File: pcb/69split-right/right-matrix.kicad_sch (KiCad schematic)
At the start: 80 parts, among them SW1 Y, SW10 I, SW11 K, SW12 <,,, SW13 Alt, SW14 (,9,,F9, SW15 O, SW16 L, SW17 >,., SW18 Fn, SW19 ),0,,F10, SW2 H, SW20 P, SW21 :,;, SW22 ?,/, SW23 Ctrl, SW24 _,-,,F11, SW25 {,[, SW26 ",', SW27 Shift, SW28 ←, SW29 +,=,,F12, SW3 N, SW30 },], SW31 Enter, SW32 ↑, SW33 ↓, SW34 Backspace, SW35 |,\, SW36 Home,PgUp, SW37 End,PgDn, SW38 →, SW39 Delete,Insert, SW4 Space, SW40 ~~,`, SW5 &,7,,F7, SW6 U, SW7 J, SW8 M, SW9 *,8,,F8

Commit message: Started layout?
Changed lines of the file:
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@@
 	)
 	(bus_entry
-		(at 196.85 134.62)
+		(at 199.39 134.62)
 		(size -2.54 2.54)
 		(stroke
@@
 	)
 	(bus_entry
-		(at 215.9 134.62)
+		(at 218.44 134.62)
 		(size -2.54 2.54)
 		(stroke
@@
 	)
 	(bus_entry
-		(at 156.21 134.62)
+		(at 158.75 134.62)
 		(size -2.54 2.54)
 		(stroke
@@
 	)
 	(bus_entry
-		(at 176.53 134.62)
+		(at 179.07 134.62)
 		(size -2.54 2.54)
 		(stroke
@@
 	)
 	(bus_entry
-		(at 137.16 134.62)
+		(at 139.7 134.62)
 		(size -2.54 2.54)
 		(stroke
@@
 	(bus
 		(pts
-			(xy 134.62 137.16) (xy 153.67 137.16)
-		)
-		(stroke
-			(width 0)
-			(type default)
-		)
-	)
-	(bus
-		(pts
-			(xy 173.99 137.16) (xy 194.31 137.16)
+			(xy 137.16 137.16) (xy 156.21 137.16)
+		)
+		(stroke
+			(width 0)
+			(type default)
+		)
+	)
+	(bus
+		(pts
+			(xy 176.53 137.16) (xy 196.85 137.16)
 		)
 		(stroke
@@
 	(bus
 		(pts
-			(xy 194.31 137.16) (xy 213.36 137.16)
+			(xy 196.85 137.16) (xy 215.9 137.16)
 		)
 		(stroke
@@
 	(bus
 		(pts
-			(xy 153.67 137.16) (xy 173.99 137.16)
+			(xy 156.21 137.16) (xy 176.53 137.16)
 		)
 		(stroke
@@
 	(bus
 		(pts
-			(xy 213.36 137.16) (xy 234.95 137.16)
+			(xy 215.9 137.16) (xy 234.95 137.16)
 		)
 		(stroke
@@
 	(bus
 		(pts
-			(xy 115.57 137.16) (xy 134.62 137.16)
-		)
-		(stroke
+			(xy 115.57 137.16) (xy 137.16 137.16)
+		)
+		(stroke

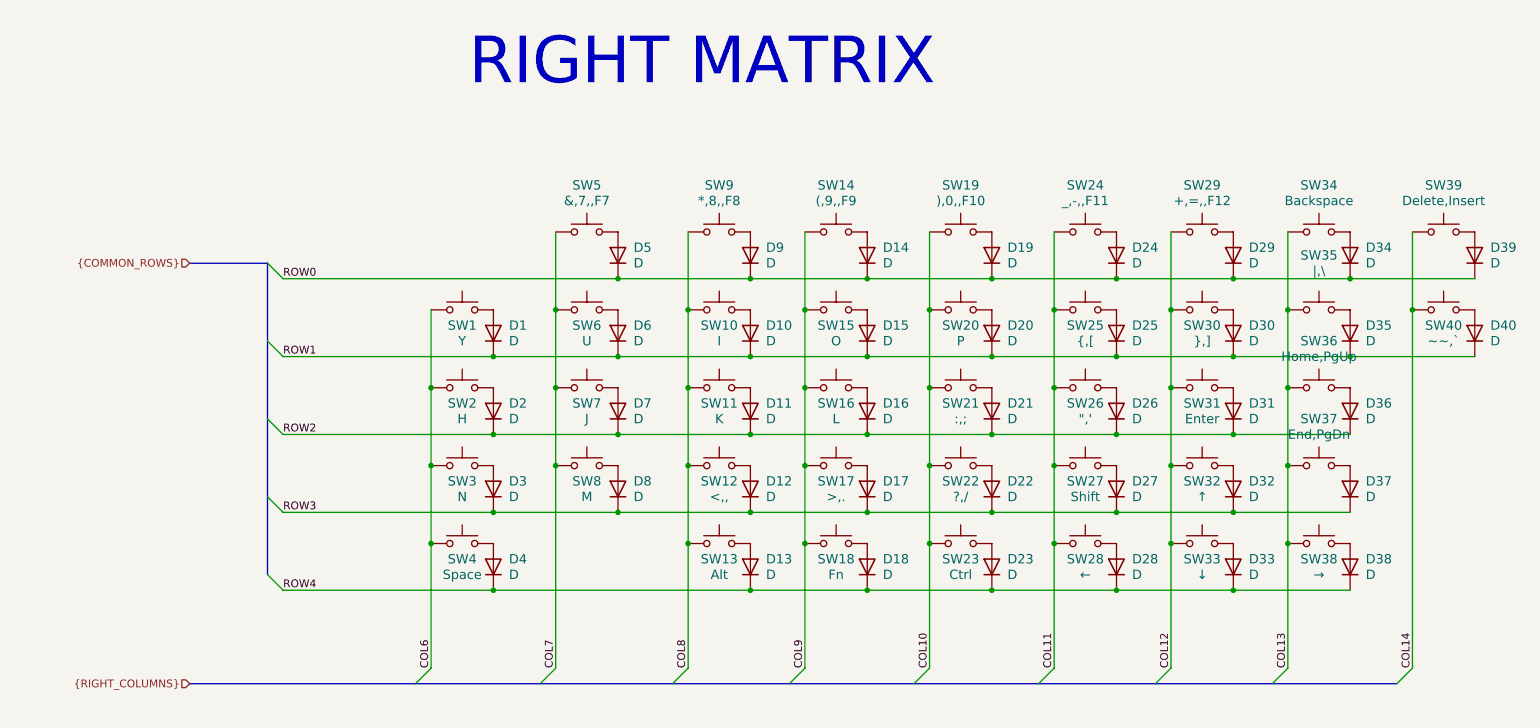
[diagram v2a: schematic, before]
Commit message: Started changing things gain to use an I/O expander with I2C.
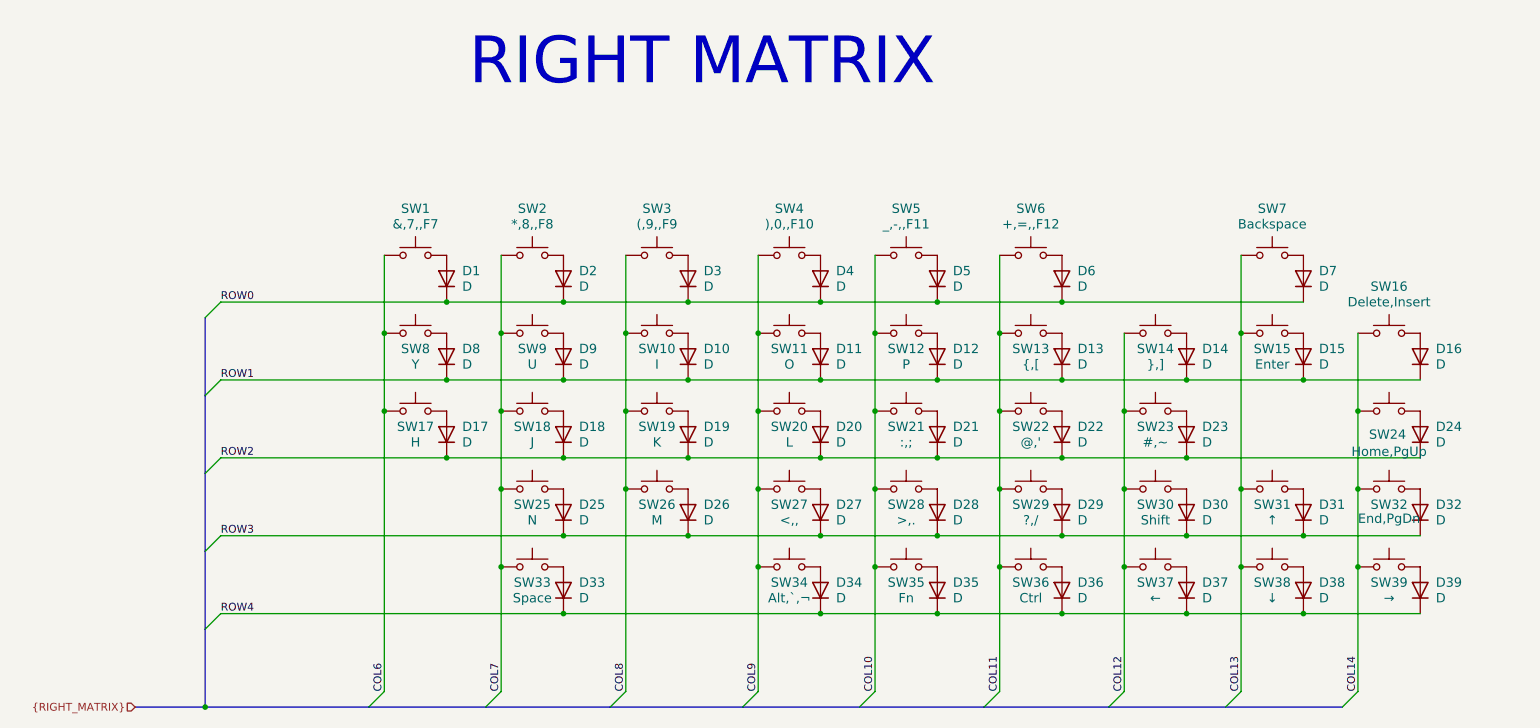
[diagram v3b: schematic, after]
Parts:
- removed D39: D, Diode_SMD:D_0805_2012Metric_Pad1.15x1.40mm_HandSolder, symbol Device:D
- removed SW40: ~~,`, Button_Switch_Keyboard:SW_Cherry_MX_1.00u_PCB, symbol Switch:SW_Push
- D1: renamed from D5; footprint Diode_SMD:D_0805_2012Metric_Pad1.15x1.40mm_HandSolder -> Diode_THT:D_DO-35_SOD27_P7.62mm_Horizontal; MPN TS4148 RBG -> 1N4454
- D10, D21: footprint Diode_SMD:D_0805_2012Metric_Pad1.15x1.40mm_HandSolder -> Diode_THT:D_DO-35_SOD27_P7.62mm_Horizontal; MPN TS4148 RBG -> 1N4454
- D11: renamed from D15; footprint Diode_SMD:D_0805_2012Metric_Pad1.15x1.40mm_HandSolder -> Diode_THT:D_DO-35_SOD27_P7.62mm_Horizontal; MPN TS4148 RBG -> 1N4454
- D12: renamed from D20; footprint Diode_SMD:D_0805_2012Metric_Pad1.15x1.40mm_HandSolder -> Diode_THT:D_DO-35_SOD27_P7.62mm_Horizontal; MPN TS4148 RBG -> 1N4454
- D13: renamed from D25; footprint Diode_SMD:D_0805_2012Metric_Pad1.15x1.40mm_HandSolder -> Diode_THT:D_DO-35_SOD27_P7.62mm_Horizontal; MPN TS4148 RBG -> 1N4454
- D14: renamed from D30; footprint Diode_SMD:D_0805_2012Metric_Pad1.15x1.40mm_HandSolder -> Diode_THT:D_DO-35_SOD27_P7.62mm_Horizontal; MPN TS4148 RBG -> 1N4454
- D15: renamed from D40; footprint Diode_SMD:D_0805_2012Metric_Pad1.15x1.40mm_HandSolder -> Diode_THT:D_DO-35_SOD27_P7.62mm_Horizontal; MPN TS4148 RBG -> 1N4454
- D16: renamed from D36; footprint Diode_SMD:D_0805_2012Metric_Pad1.15x1.40mm_HandSolder -> Diode_THT:D_DO-35_SOD27_P7.62mm_Horizontal; MPN TS4148 RBG -> 1N4454
- D17: renamed from D2; footprint Diode_SMD:D_0805_2012Metric_Pad1.15x1.40mm_HandSolder -> Diode_THT:D_DO-35_SOD27_P7.62mm_Horizontal; MPN TS4148 RBG -> 1N4454
- D18: renamed from D7; footprint Diode_SMD:D_0805_2012Metric_Pad1.15x1.40mm_HandSolder -> Diode_THT:D_DO-35_SOD27_P7.62mm_Horizontal; MPN TS4148 RBG -> 1N4454
- D19: renamed from D11; footprint Diode_SMD:D_0805_2012Metric_Pad1.15x1.40mm_HandSolder -> Diode_THT:D_DO-35_SOD27_P7.62mm_Horizontal; MPN TS4148 RBG -> 1N4454
- D2: renamed from D9; footprint Diode_SMD:D_0805_2012Metric_Pad1.15x1.40mm_HandSolder -> Diode_THT:D_DO-35_SOD27_P7.62mm_Horizontal; MPN TS4148 RBG -> 1N4454
- D20: renamed from D16; footprint Diode_SMD:D_0805_2012Metric_Pad1.15x1.40mm_HandSolder -> Diode_THT:D_DO-35_SOD27_P7.62mm_Horizontal; MPN TS4148 RBG -> 1N4454
- D22: renamed from D26; footprint Diode_SMD:D_0805_2012Metric_Pad1.15x1.40mm_HandSolder -> Diode_THT:D_DO-35_SOD27_P7.62mm_Horizontal; MPN TS4148 RBG -> 1N4454
- D23: renamed from D31; footprint Diode_SMD:D_0805_2012Metric_Pad1.15x1.40mm_HandSolder -> Diode_THT:D_DO-35_SOD27_P7.62mm_Horizontal; MPN TS4148 RBG -> 1N4454
- D24: renamed from D37; footprint Diode_SMD:D_0805_2012Metric_Pad1.15x1.40mm_HandSolder -> Diode_THT:D_DO-35_SOD27_P7.62mm_Horizontal; MPN TS4148 RBG -> 1N4454
- D25: renamed from D3; footprint Diode_SMD:D_0805_2012Metric_Pad1.15x1.40mm_HandSolder -> Diode_THT:D_DO-35_SOD27_P7.62mm_Horizontal; MPN TS4148 RBG -> 1N4454
- D26: renamed from D8; footprint Diode_SMD:D_0805_2012Metric_Pad1.15x1.40mm_HandSolder -> Diode_THT:D_DO-35_SOD27_P7.62mm_Horizontal; MPN TS4148 RBG -> 1N4454
- D27: renamed from D12; footprint Diode_SMD:D_0805_2012Metric_Pad1.15x1.40mm_HandSolder -> Diode_THT:D_DO-35_SOD27_P7.62mm_Horizontal; MPN TS4148 RBG -> 1N4454
- D28: renamed from D17; footprint Diode_SMD:D_0805_2012Metric_Pad1.15x1.40mm_HandSolder -> Diode_THT:D_DO-35_SOD27_P7.62mm_Horizontal; MPN TS4148 RBG -> 1N4454
- D29: renamed from D22; footprint Diode_SMD:D_0805_2012Metric_Pad1.15x1.40mm_HandSolder -> Diode_THT:D_DO-35_SOD27_P7.62mm_Horizontal; MPN TS4148 RBG -> 1N4454
- D3: renamed from D14; footprint Diode_SMD:D_0805_2012Metric_Pad1.15x1.40mm_HandSolder -> Diode_THT:D_DO-35_SOD27_P7.62mm_Horizontal; MPN TS4148 RBG -> 1N4454
- D30: renamed from D27; footprint Diode_SMD:D_0805_2012Metric_Pad1.15x1.40mm_HandSolder -> Diode_THT:D_DO-35_SOD27_P7.62mm_Horizontal; MPN TS4148 RBG -> 1N4454
- D31: renamed from D32; footprint Diode_SMD:D_0805_2012Metric_Pad1.15x1.40mm_HandSolder -> Diode_THT:D_DO-35_SOD27_P7.62mm_Horizontal; MPN TS4148 RBG -> 1N4454
- D32: renamed from D35; footprint Diode_SMD:D_0805_2012Metric_Pad1.15x1.40mm_HandSolder -> Diode_THT:D_DO-35_SOD27_P7.62mm_Horizontal; MPN TS4148 RBG -> 1N4454
- D33: renamed from D4; footprint Diode_SMD:D_0805_2012Metric_Pad1.15x1.40mm_HandSolder -> Diode_THT:D_DO-35_SOD27_P7.62mm_Horizontal; MPN TS4148 RBG -> 1N4454
- D34: renamed from D13; footprint Diode_SMD:D_0805_2012Metric_Pad1.15x1.40mm_HandSolder -> Diode_THT:D_DO-35_SOD27_P7.62mm_Horizontal; MPN TS4148 RBG -> 1N4454
- D35: renamed from D18; footprint Diode_SMD:D_0805_2012Metric_Pad1.15x1.40mm_HandSolder -> Diode_THT:D_DO-35_SOD27_P7.62mm_Horizontal; MPN TS4148 RBG -> 1N4454
- D36: renamed from D23; footprint Diode_SMD:D_0805_2012Metric_Pad1.15x1.40mm_HandSolder -> Diode_THT:D_DO-35_SOD27_P7.62mm_Horizontal; MPN TS4148 RBG -> 1N4454
- D37: renamed from D28; footprint Diode_SMD:D_0805_2012Metric_Pad1.15x1.40mm_HandSolder -> Diode_THT:D_DO-35_SOD27_P7.62mm_Horizontal; MPN TS4148 RBG -> 1N4454
- D38: renamed from D33; footprint Diode_SMD:D_0805_2012Metric_Pad1.15x1.40mm_HandSolder -> Diode_THT:D_DO-35_SOD27_P7.62mm_Horizontal; MPN TS4148 RBG -> 1N4454
- D39: renamed from D38; footprint Diode_SMD:D_0805_2012Metric_Pad1.15x1.40mm_HandSolder -> Diode_THT:D_DO-35_SOD27_P7.62mm_Horizontal; MPN TS4148 RBG -> 1N4454
- D4: renamed from D19; footprint Diode_SMD:D_0805_2012Metric_Pad1.15x1.40mm_HandSolder -> Diode_THT:D_DO-35_SOD27_P7.62mm_Horizontal; MPN TS4148 RBG -> 1N4454
- D5: renamed from D24; footprint Diode_SMD:D_0805_2012Metric_Pad1.15x1.40mm_HandSolder -> Diode_THT:D_DO-35_SOD27_P7.62mm_Horizontal; MPN TS4148 RBG -> 1N4454
- D6: renamed from D29; footprint Diode_SMD:D_0805_2012Metric_Pad1.15x1.40mm_HandSolder -> Diode_THT:D_DO-35_SOD27_P7.62mm_Horizontal; MPN TS4148 RBG -> 1N4454
- D7: renamed from D34; footprint Diode_SMD:D_0805_2012Metric_Pad1.15x1.40mm_HandSolder -> Diode_THT:D_DO-35_SOD27_P7.62mm_Horizontal; MPN TS4148 RBG -> 1N4454
- D8: renamed from D1; footprint Diode_SMD:D_0805_2012Metric_Pad1.15x1.40mm_HandSolder -> Diode_THT:D_DO-35_SOD27_P7.62mm_Horizontal; MPN TS4148 RBG -> 1N4454
- D9: renamed from D6; footprint Diode_SMD:D_0805_2012Metric_Pad1.15x1.40mm_HandSolder -> Diode_THT:D_DO-35_SOD27_P7.62mm_Horizontal; MPN TS4148 RBG -> 1N4454
- SW15: renamed from SW35; value |,\ -> Enter; footprint Button_Switch_Keyboard:SW_Cherry_MX_1.50u_PCB -> Button_Switch_Keyboard:SW_Cherry_MX_ISOEnter_PCB
- SW22: renamed from SW26; value ",' -> @,'
- SW23: renamed from SW31; value Enter -> #,~; footprint Button_Switch_Keyboard:SW_Cherry_MX_2.25u_PCB -> Button_Switch_Keyboard:SW_Cherry_MX_1.00u_PCB
- SW34: renamed from SW13; value Alt -> Alt,`,¬; footprint Button_Switch_Keyboard:SW_Cherry_MX_1.00u_PCB -> Button_Switch_Keyboard:SW_Cherry_MX_1.25u_PCB
- SW35: renamed from SW18; footprint Button_Switch_Keyboard:SW_Cherry_MX_1.00u_PCB -> Button_Switch_Keyboard:SW_Cherry_MX_1.25u_PCB
- SW36: renamed from SW23; footprint Button_Switch_Keyboard:SW_Cherry_MX_1.00u_PCB -> Button_Switch_Keyboard:SW_Cherry_MX_1.25u_PCB
- renumbered SW5 to SW1, SW15 to SW11, SW20 to SW12, SW25 to SW13, SW30 to SW14, SW39 to SW16, SW2 to SW17, SW7 to SW18, SW11 to SW19, SW9 to SW2, SW16 to SW20, SW36 to SW24, SW3 to SW25, SW8 to SW26, SW12 to SW27, SW17 to SW28, SW22 to SW29, SW14 to SW3, SW27 to SW30, SW32 to SW31, SW37 to SW32, SW4 to SW33, SW28 to SW37, SW33 to SW38, SW38 to SW39, SW19 to SW4, SW24 to SW5, SW29 to SW6, SW34 to SW7, SW1 to SW8, SW6 to SW9
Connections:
- net COL10: now also SW28.1, SW35.1, SW5.1; no longer SW29.1, SW36.1, SW4.1
- net COL11: now also SW29.1, SW36.1, SW6.1; no longer SW30.1, SW37.1, SW5.1
- net COL12: now also SW30.1, SW37.1; no longer SW31.1, SW38.1, SW6.1
- net COL13: now also SW31.1, SW38.1; no longer SW24.1, SW32.1, SW39.1
- net COL14: now also SW24.1, SW32.1, SW39.1
- net COL6: now also SW1.1; no longer SW25.1, SW33.1
- net COL7: now also SW2.1, SW25.1, SW33.1; no longer SW1.1, SW26.1
- net COL8: now also SW26.1, SW3.1; no longer SW2.1, SW27.1, SW34.1
- net COL9: now also SW27.1, SW34.1, SW4.1; no longer SW28.1, SW3.1, SW35.1
- net ROW1: now also D16.1 (K); no longer D32.1 (K)
- net ROW2: now also D24.1 (K); no longer D16.1 (K)
- net ROW3: now also D32.1 (K); no longer D24.1 (K)
- net at D15.2 (A): now also SW15.2
- net at D32.2 (A): now also SW32.2; no longer SW15.2
- net at SW16.2: now also D16.2 (A)
- net at SW24.2: now also D24.2 (A); no longer D16.2 (A)
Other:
- company: (none) -> Yiannis Michael
- title: 69SPLIT KEYBOARD -> 69SPLIT
- moved on the sheet: D1, D10, D11, D12, D13, D14, D15, D16, D17, D18, D19, D2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

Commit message: Continuing with I/O expander integration.
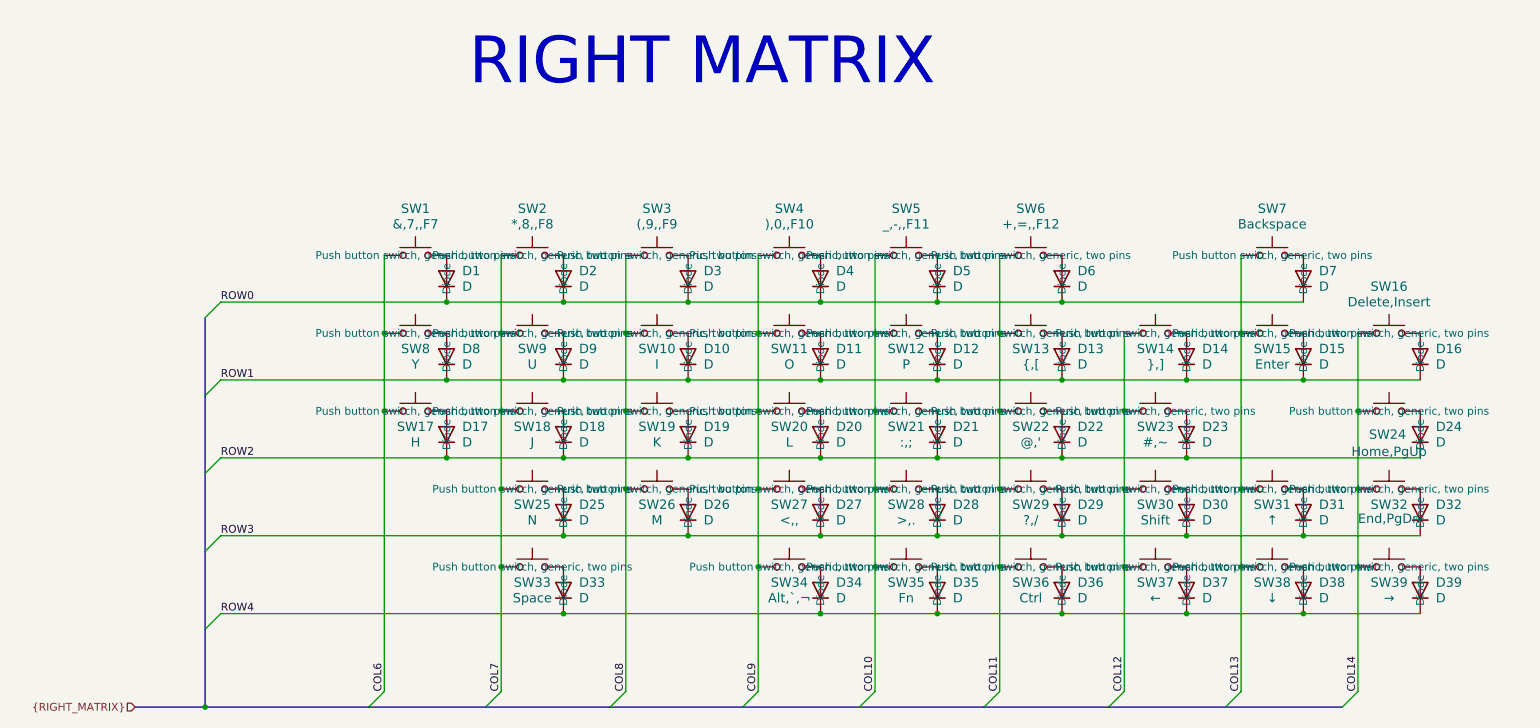
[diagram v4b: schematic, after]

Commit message: Alright I think now the left side is actually ready.
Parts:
- SW1: value &,7,,F7 -> SW_Push; Key (none) -> &,7,,F7
- SW10: renamed from SW9; value U -> SW_Push; Key (none) -> U
- SW11: renamed from SW10; value I -> SW_Push; Key (none) -> I
- SW12: renamed from SW11; value O -> SW_Push; Key (none) -> O
- SW13: renamed from SW12; value P -> SW_Push; Key (none) -> P
- SW14: renamed from SW13; value {,[ -> SW_Push; Key (none) -> {,[
- SW15: renamed from SW14; value },] -> SW_Push; Key (none) -> },]
- SW16: renamed from SW15; value Enter -> SW_Push; Key (none) -> Enter
- SW17: value H -> SW_Push; Key (none) -> H
- SW18: value J -> SW_Push; Key (none) -> J
- SW19: value K -> SW_Push; Key (none) -> K
- SW2: value *,8,,F8 -> SW_Push; Key (none) -> *,8,,F8
- SW20: value L -> SW_Push; Key (none) -> L
- SW21: value :,; -> SW_Push; Key (none) -> :,;
- SW22: value @,' -> SW_Push; Key (none) -> @,'
- SW23: value #,~ -> SW_Push; Key (none) -> #,~
- SW24: value Home,PgUp -> SW_Push; Key (none) -> Home,PgUp
- SW25: value N -> SW_Push; Key (none) -> N
- SW26: value M -> SW_Push; Key (none) -> M
- SW27: value <,, -> SW_Push; Key (none) -> <,,
- SW28: value >,. -> SW_Push; Key (none) -> >,.
- SW29: value ?,/ -> SW_Push; Key (none) -> ?,/
- SW3: value (,9,,F9 -> SW_Push; Key (none) -> (,9,,F9
- SW30: value Shift -> SW_Push; Key (none) -> Shift
- SW31: value ↑ -> SW_Push; Key (none) -> ↑
- SW32: value End,PgDn -> SW_Push; Key (none) -> End,PgDn
- SW33: value Space -> SW_Push; Key (none) -> Space
- SW34: value Alt,`,¬ -> SW_Push; Key (none) -> Alt,`,¬
- SW35: value Fn -> SW_Push; Key (none) -> Fn
- SW36: value Ctrl -> SW_Push; Key (none) -> Ctrl
- SW37: value ← -> SW_Push; Key (none) -> ←
- SW38: value ↓ -> SW_Push; Key (none) -> ↓
- SW39: value → -> SW_Push; Key (none) -> →
- SW4: value ),0,,F10 -> SW_Push; Key (none) -> ),0,,F10
- SW5: value _,-,,F11 -> SW_Push; Key (none) -> _,-,,F11
- SW6: value +,=,,F12 -> SW_Push; Key (none) -> +,=,,F12
- SW7: value Backspace -> SW_Push; Key (none) -> Backspace
- SW8: renamed from SW16; value Delete,Insert -> SW_Push; Key (none) -> Delete,Insert
- SW9: renamed from SW8; value Y -> SW_Push; Key (none) -> Y
- renumbered D9 to D10, D10 to D11, D11 to D12, D12 to D13, D13 to D14, D14 to D15, D15 to D16, D16 to D8, D8 to D9
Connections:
- net COL14 is gone; now on net COL13: SW24.1, SW32.1, SW39.1, SW8.1
- net COL10: now also SW29.1, SW36.1; no longer SW28.1, SW35.1
- net COL11: now also SW30.1, SW37.1; no longer SW29.1, SW36.1
- net COL12: now also SW31.1, SW38.1, SW7.1; no longer SW30.1, SW37.1
- net COL13: no longer SW31.1, SW38.1, SW7.1
- net COL6: now also SW25.1, SW33.1
- net COL7: now also SW26.1; no longer SW25.1, SW33.1
- net COL8: now also SW27.1, SW34.1; no longer SW26.1
- net COL9: now also SW28.1, SW35.1; no longer SW27.1, SW34.1
- net ROW0: now also D8.1 (K)
- net ROW1: no longer D8.1 (K)
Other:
- moved on the sheet: D24, D25, D26, D27, D28, D29, D30, D31, D32, D33, D34, D35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

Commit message: Final touches.
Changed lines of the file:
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@@
 		(title "69SPLIT")
 		(date "2025-07-28")
-		(rev "1")
+		(rev "A")
 		(company "Yiannis Michael")
 		(comment 1 "Yiannis Michael")
@@
 	)
 	(hierarchical_label "{RIGHT_MATRIX}"
-		(shape input)
+		(shape bidirectional)
 		(at 49.53 140.97 180)
 		(effects
